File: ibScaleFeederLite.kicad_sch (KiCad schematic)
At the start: 86 parts, among them J1 PEEL, J2 DRIVE, J3 RAIL, J4 SWD, J5 Serial, SW1 DOWN, SW2 UP, SW3 BOOT, U2 DRV8837, U3 DRV8837, U4 THVD1400D, U5 TPS563300, U6 AMS1117-3.3, U9 STM32F031C6Tx, Y1 8MHz

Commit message: Add SWD header to back of board for in-place debug of a running feeder.
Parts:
- added J6: SWD, Connector_PinHeader_1.27mm:PinHeader_2x05_P1.27mm_Vertical_SMD, symbol Connector:Conn_ARM_JTAG_SWD_10
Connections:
- net +3.3V: now also J6.1 (VTref)
- net GND: now also J6.3 (GND), J6.5 (GND), J6.9 (GNDDetect)
- net SWCLK: now also J6.4 (SWCLK/TCK)
- net SWDIO: now also J6.2 (SWDIO/TMS)
- net ~{RESET}: now also J6.10 (~{RESET})
- no-connect marks 22 -> 24

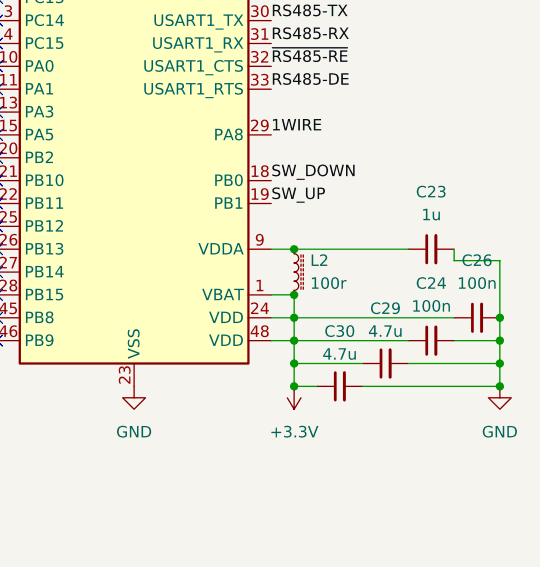
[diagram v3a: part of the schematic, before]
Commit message: Change VDDA ferrite to 120-ohm for better parts availability
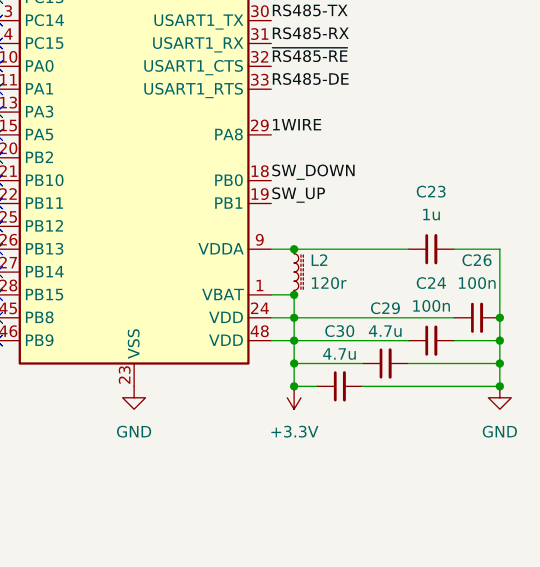
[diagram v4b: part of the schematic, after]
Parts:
- L2: value 100r -> 120r; DigiKey 445-MPZ1608Y101BTA00CT-ND -> 283-MFBM1V1608-121-RCT-ND; LCSC C501996 -> C14709; Manufacturer_Name TDK -> Eaton; Manufacturer_Part MPZ1608Y101BTA00 -> MFBM1V1608-121-R; Mouser 810-MPZ1608Y101BTA00 -> 704-MFBM1V1608-121-R
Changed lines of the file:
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@@
 	(wire
 		(pts
-			(xy 332.74 161.29) (xy 332.74 167.64)
+			(xy 332.74 160.02) (xy 332.74 167.64)
 		)
 		(stroke
@@
 	(wire
 		(pts
-			(xy 327.66 160.02) (xy 327.66 161.29)
-		)
-		(stroke
-			(width 0)
-			(type default)
-		)
-	)
-	(wire
-		(pts
 			(xy 43.18 96.52) (xy 43.18 97.79)
 		)
@@
 	(wire
 		(pts
-			(xy 327.66 161.29) (xy 332.74 161.29)
+			(xy 327.66 160.02) (xy 332.74 160.02)
 		)
 		(stroke
@@
 			)
 		)
-		(property "Value" "100r"
+		(property "Value" "120r"
 			(at 311.658 163.83 0)
 			(show_name no)
@@
 			)
 		)
-		(property "Manufacturer_Name" "TDK"
+		(property "Manufacturer_Name" "Eaton"
 			(at 309.88 162.56 0)
 			(hide yes)
@@
 			)
 		)
-		(property "LCSC" "C501996"
+		(property "LCSC" "C14709"
 			(at 309.88 162.56 0)
 			(hide yes)
@@
 			)
 		)
-		(property "Mouser" "810-MPZ1608Y101BTA00"
+		(property "Mouser" "704-MFBM1V1608-121-R"
 			(at 309.88 162.56 0)
 			(hide yes)
@@
 			)
 		)
-		(property "Manufacturer_Part" "MPZ1608Y101BTA00"
+		(property "Manufacturer_Part" "MFBM1V1608-121-R"
 			(at 309.88 162.56 0)
 			(hide yes)
@@
 			)
 		)
-		(property "DigiKey" "445-MPZ1608Y101BTA00CT-ND"
+		(property "DigiKey" "283-MFBM1V1608-121-RCT-ND"
 			(at 309.88 162.56 0)
 			(hide yes)
@@
 			(at 149.86 106.68 0)
 			(hide yes)
+			(show_name no)
+			(do_not_autoplace no)
+			(effects
+				(font
+					(size 1.27 1.27)
+				)
+			)
+		)
+		(property "Tolerance" ""
+			(at 149.86 106.68 0)
+			(hide yes)
+			(show_name no)
+			(do_not_autoplace no)
+			(effects
+				(font
+					(size 1.27 1.27)
+				)
+			)
+		)
+		(property "Rating" ""
+			(at 149.86 106.68 0)
+			(hide yes)
+			(show_name no)
+			(do_not_autoplace no)
+			(effects
+				(font
+					(size 1.27 1.27)
+				)
+			)
+		)
+		(property "Notes" ""
+			(at 149.86 106.68 0)
+			(hide yes)

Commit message: update L1 to use correct VLX4045EX footprint instead of generic one
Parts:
- L1: footprint Inductor_SMD:L_6.3x6.3_H3 -> Inductor_SMD:L_TDK_VLS6045EX_VLS6045AF
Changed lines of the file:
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@@
 			)
 		)
-		(property "Footprint" "Inductor_SMD:L_6.3x6.3_H3"
+		(property "Footprint" "Inductor_SMD:L_TDK_VLS6045EX_VLS6045AF"
 			(at 63.5 35.56 0)
 			(hide yes)
